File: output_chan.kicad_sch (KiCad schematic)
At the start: 12 parts, among them U2 MAX14917AFM+

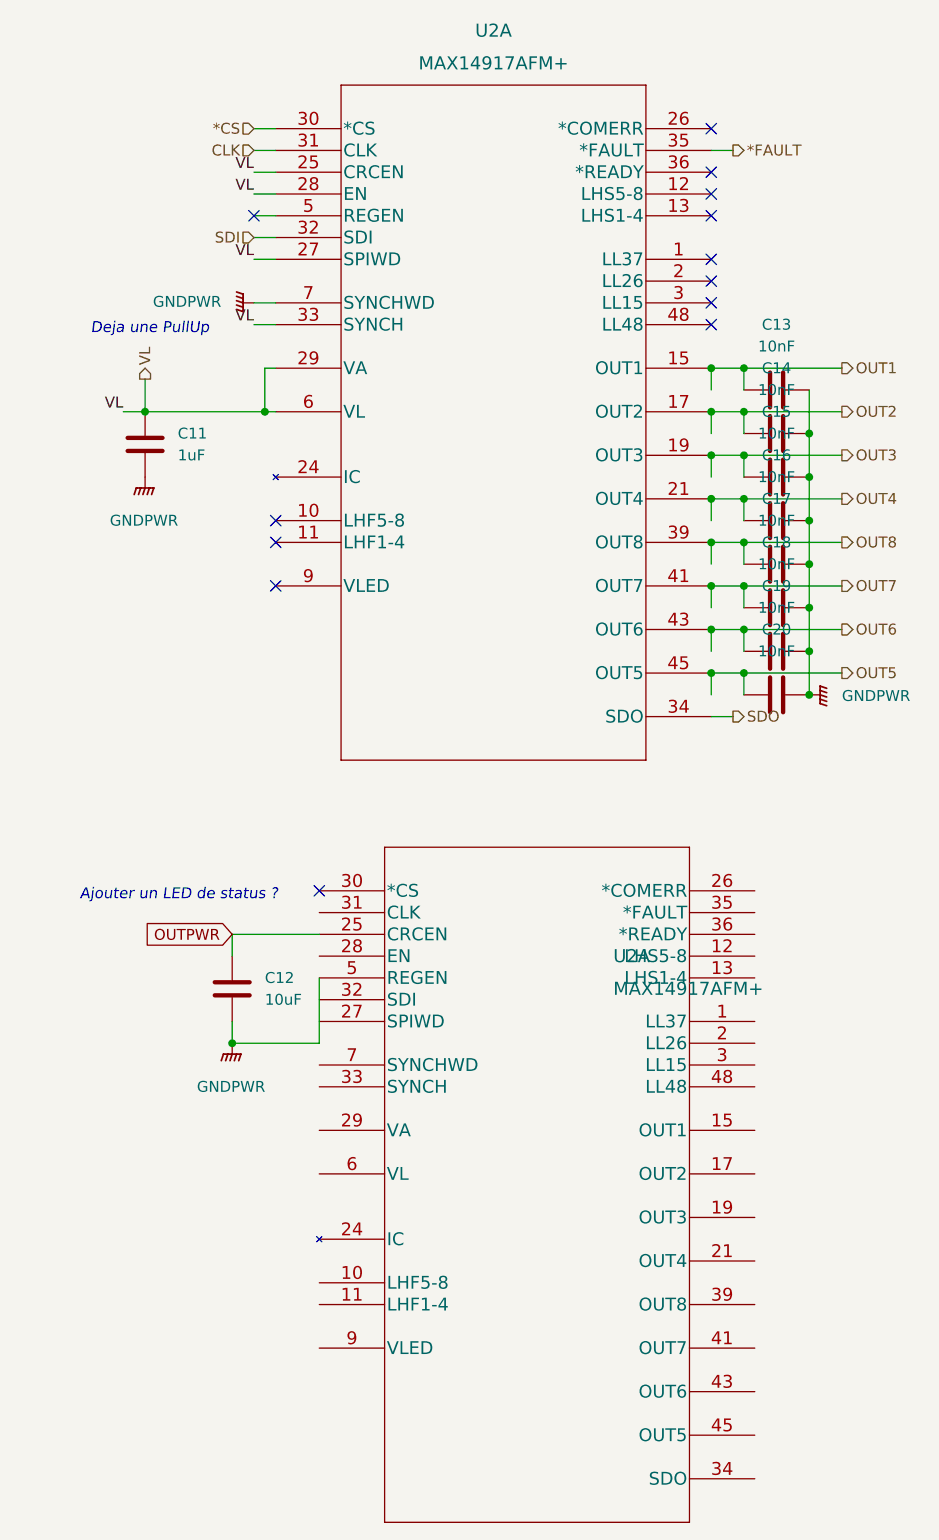
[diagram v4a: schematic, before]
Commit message: Basic routing done, cheating a bit on the diff + add holes (to be positionned)
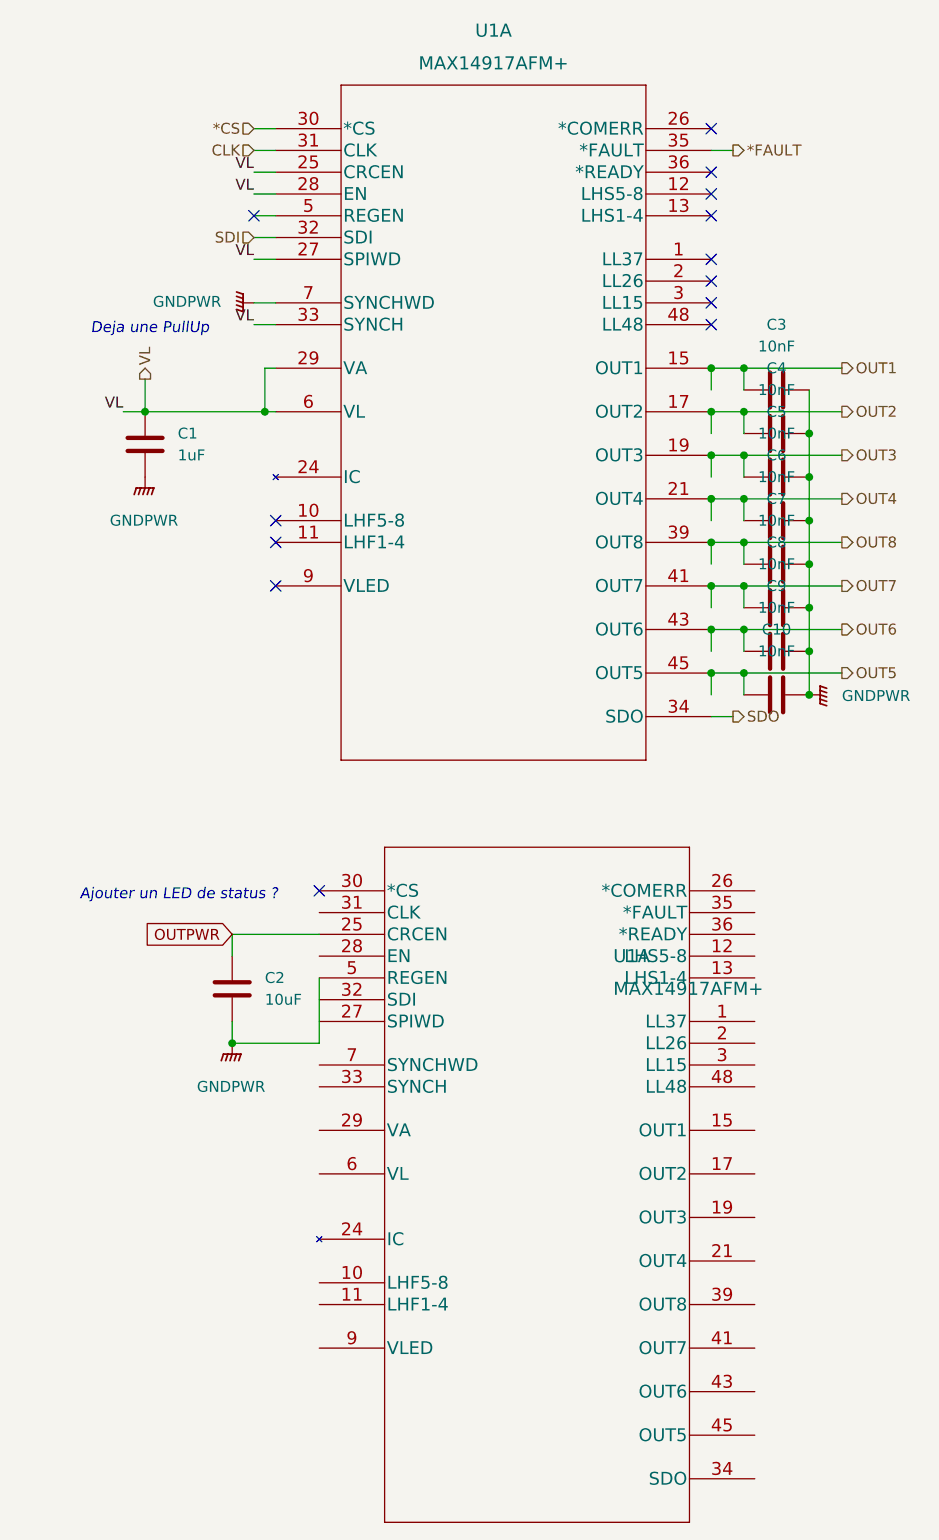
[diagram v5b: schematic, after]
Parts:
- renumbered C11 to C1, C20 to C10, C12 to C2, C13 to C3, C14 to C4, C15 to C5, C16 to C6, C17 to C7, C18 to C8, C19 to C9, U2 to U1
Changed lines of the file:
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@@
   (symbol (lib_id "power:GNDPWR") (at 189.23 109.22 90)
     (in_bom yes) (on_board yes) (fields_autoplaced)
-    (property "Reference" "#PWR08" (id 0) (at 194.31 109.22 0)
+    (property "Reference" "#PWR04" (id 0) (at 194.31 109.22 0)
       (effects (font (size 1.27 1.27)) hide)
     )
@@
   (symbol (lib_id "Device:C") (at 111.76 80.01 0)
     (in_bom yes) (on_board yes) (fields_autoplaced)
-    (property "Reference" "C11" (id 0) (at 115.57 78.7399 0)
+    (property "Reference" "C1" (id 0) (at 115.57 78.7399 0)
       (effects (font (size 1.27 1.27)) (justify left))
     )
@@
   (symbol (lib_id "power:GNDPWR") (at 111.76 83.82 0)
     (in_bom yes) (on_board yes) (fields_autoplaced)
-    (property "Reference" "#PWR05" (id 0) (at 111.76 88.9 0)
+    (property "Reference" "#PWR01" (id 0) (at 111.76 88.9 0)
       (effects (font (size 1.27 1.27)) hide)
     )
@@
   (symbol (lib_id "Maxim industrial IO:MAX14917AFM+") (at 127 43.18 0)
     (in_bom yes) (on_board yes) (fields_autoplaced)
-    (property "Reference" "U2" (id 0) (at 152.4 31.75 0)
+    (property "Reference" "U1" (id 0) (at 152.4 31.75 0)
       (effects (font (size 1.524 1.524)))
     )
@@
   (symbol (lib_id "Device:C") (at 185.42 83.82 90)
     (in_bom yes) (on_board yes) (fields_autoplaced)
-    (property "Reference" "C15" (id 0) (at 185.42 76.2 90))
+    (property "Reference" "C5" (id 0) (at 185.42 76.2 90))
     (property "Value" "10nF" (id 1) (at 185.42 78.74 90))
     (property "Footprint" "Capacitor_SMD:C_0603_1608Metric" (id 2) (at 189.23 82.8548 0)
@@
   (symbol (lib_id "Device:C") (at 185.42 88.9 90)
     (in_bom yes) (on_board yes) (fields_autoplaced)
-    (property "Reference" "C16" (id 0) (at 185.42 81.28 90))
+    (property "Reference" "C6" (id 0) (at 185.42 81.28 90))
     (property "Value" "10nF" (id 1) (at 185.42 83.82 90))
     (property "Footprint" "Capacitor_SMD:C_0603_1608Metric" (id 2) (at 189.23 87.9348 0)
@@
   (symbol (lib_id "Device:C") (at 185.42 78.74 90)
     (in_bom yes) (on_board yes) (fields_autoplaced)
-    (property "Reference" "C14" (id 0) (at 185.42 71.12 90))
+    (property "Reference" "C4" (id 0) (at 185.42 71.12 90))
     (property "Value" "10nF" (id 1) (at 185.42 73.66 90))
     (property "Footprint" "Capacitor_SMD:C_0603_1608Metric" (id 2) (at 189.23 77.7748 0)
@@
   (symbol (lib_id "Device:C") (at 185.42 104.14 90)
     (in_bom yes) (on_board yes) (fields_autoplaced)
-    (property "Reference" "C19" (id 0) (at 185.42 96.52 90))
+    (property "Reference" "C9" (id 0) (at 185.42 96.52 90))
     (property "Value" "10nF" (id 1) (at 185.42 99.06 90))
     (property "Footprint" "Capacitor_SMD:C_0603_1608Metric" (id 2) (at 189.23 103.1748 0)
@@
   (symbol (lib_id "power:GNDPWR") (at 124.46 63.5 270)
     (in_bom yes) (on_board yes) (fields_autoplaced)
-    (property "Reference" "#PWR07" (id 0) (at 119.38 63.5 0)
+    (property "Reference" "#PWR03" (id 0) (at 119.38 63.5 0)
       (effects (font (size 1.27 1.27)) hide)
     )
@@
   (symbol (lib_id "Maxim industrial IO:MAX14917AFM+") (at 132.08 132.08 0)
     (in_bom yes) (on_board yes) (fields_autoplaced)
-    (property "Reference" "U2" (id 0) (at 166.37 139.7 0)
+    (property "Reference" "U1" (id 0) (at 166.37 139.7 0)
       (effects (font (size 1.524 1.524)) (justify left))
     )
@@
       (effects (font (size 1.524 1.524)))
     )
-    (pin "1")
-    (pin "10")
-    (pin "11")
-    (pin "12")
-    (pin "13")
-    (pin "15")
-    (pin "16")
-    (pin "17")
-    (pin "18")
-    (pin "19")
-    (pin "2")
-    (pin "20")
-    (pin "21")
-    (pin "22")
-    (pin "24")
-    (pin "25")
-    (pin "26")
-    (pin "27")
-    (pin "28")
-    (pin "29")
-    (pin "3")
-    (pin "30")
-    (pin "31")
-    (pin "32")
-    (pin "33")
-    (pin "34")
-    (pin "35")
-    (pin "36")
-    (pin "37")
-    (pin "39")
-    (pin "40")
-    (pin "41")
-    (pin "42")
-    (pin "43")
-    (pin "44")
-    (pin "45")
-    (pin "46")
-    (pin "48")
-    (pin "5")
-    (pin "6")
-    (pin "7")
-    (pin "9")
+    (pin "14")
+    (pin "23")
+    (pin "38")
+    (pin "4")
+    (pin "47")
+    (pin "49")
+    (pin "8")
   )
   (symbol (lib_id "Device:C") (at 185.42 93.98 90)
     (in_bom yes) (on_board yes) (fields_autoplaced)
-    (property "Reference" "C17" (id 0) (at 185.42 86.36 90))
+    (property "Reference" "C7" (id 0) (at 185.42 86.36 90))
     (property "Value" "10nF" (id 1) (at 185.42 88.9 90))
     (property "Footprint" "Capacitor_SMD:C_0603_1608Metric" (id 2) (at 189.23 93.0148 0)
@@
   (symbol (lib_id "Device:C") (at 185.42 73.66 90)
     (in_bom yes) (on_board yes) (fields_autoplaced)
-    (property "Reference" "C13" (id 0) (at 185.42 66.04 90))
+    (property "Reference" "C3" (id 0) (at 185.42 66.04 90))
     (property "Value" "10nF" (id 1) (at 185.42 68.58 90))
     (property "Footprint" "Capacitor_SMD:C_0603_1608Metric" (id 2) (at 189.23 72.6948 0)
@@
   (symbol (lib_id "Device:C") (at 185.42 99.06 90)
     (in_bom yes) (on_board yes) (fields_autoplaced)
-    (property "Reference" "C18" (id 0) (at 185.42 91.44 90))
+    (property "Reference" "C8" (id 0) (at 185.42 91.44 90))
     (property "Value" "10nF" (id 1) (at 185.42 93.98 90))
     (property "Footprint" "Capacitor_SMD:C_0603_1608Metric" (id 2) (at 189.23 98.0948 0)
@@
   (symbol (lib_id "power:GNDPWR") (at 121.92 149.86 0)
     (in_bom yes) (on_board yes) (fields_autoplaced)
-    (property "Reference" "#PWR06" (id 0) (at 121.92 154.94 0)
+    (property "Reference" "#PWR02" (id 0) (at 121.92 154.94 0)
       (effects (font (size 1.27 1.27)) hide)
     )
@@
   (symbol (lib_id "Device:C") (at 121.92 143.51 0)
     (in_bom yes) (on_board yes) (fields_autoplaced)
-    (property "Reference" "C12" (id 0) (at 125.73 142.2399 0)
+    (property "Reference" "C2" (id 0) (at 125.73 142.2399 0)
       (effects (font (size 1.27 1.27)) (justify left))
     )
@@
   (symbol (lib_id "Device:C") (at 185.42 109.22 90)
     (in_bom yes) (on_board yes) (fields_autoplaced)
-    (property "Reference" "C20" (id 0) (at 185.42 101.6 90))
+    (property "Reference" "C10" (id 0) (at 185.42 101.6 90))
     (property "Value" "10nF" (id 1) (at 185.42 104.14 90))
     (property "Footprint" "Capacitor_SMD:C_0603_1608Metric" (id 2) (at 189.23 108.2548 0)

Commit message: fix most errors/warnings
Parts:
- renumbered C1 to C23, C2 to C24, C3 to C25, C4 to C26, C5 to C27, C6 to C28, C7 to C29, C8 to C30, C9 to C31, C10 to C32, U1 to U4
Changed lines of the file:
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@@
   (symbol (lib_id "Device:C") (at 111.76 80.01 0)
     (in_bom yes) (on_board yes) (fields_autoplaced)
-    (property "Reference" "C1" (id 0) (at 115.57 78.7399 0)
+    (property "Reference" "C23" (id 0) (at 115.57 78.7399 0)
       (effects (font (size 1.27 1.27)) (justify left))
     )
@@
   (symbol (lib_id "Maxim industrial IO:MAX14917AFM+") (at 127 43.18 0)
     (in_bom yes) (on_board yes) (fields_autoplaced)
-    (property "Reference" "U1" (id 0) (at 152.4 31.75 0)
+    (property "Reference" "U4" (id 0) (at 152.4 31.75 0)
       (effects (font (size 1.524 1.524)))
     )
@@
   (symbol (lib_id "Device:C") (at 185.42 83.82 90)
     (in_bom yes) (on_board yes) (fields_autoplaced)
-    (property "Reference" "C5" (id 0) (at 185.42 76.2 90))
+    (property "Reference" "C27" (id 0) (at 185.42 76.2 90))
     (property "Value" "10nF" (id 1) (at 185.42 78.74 90))
     (property "Footprint" "Capacitor_SMD:C_0603_1608Metric" (id 2) (at 189.23 82.8548 0)
@@
   (symbol (lib_id "Device:C") (at 185.42 88.9 90)
     (in_bom yes) (on_board yes) (fields_autoplaced)
-    (property "Reference" "C6" (id 0) (at 185.42 81.28 90))
+    (property "Reference" "C28" (id 0) (at 185.42 81.28 90))
     (property "Value" "10nF" (id 1) (at 185.42 83.82 90))
     (property "Footprint" "Capacitor_SMD:C_0603_1608Metric" (id 2) (at 189.23 87.9348 0)
@@
   (symbol (lib_id "Device:C") (at 185.42 78.74 90)
     (in_bom yes) (on_board yes) (fields_autoplaced)
-    (property "Reference" "C4" (id 0) (at 185.42 71.12 90))
+    (property "Reference" "C26" (id 0) (at 185.42 71.12 90))
     (property "Value" "10nF" (id 1) (at 185.42 73.66 90))
     (property "Footprint" "Capacitor_SMD:C_0603_1608Metric" (id 2) (at 189.23 77.7748 0)
@@
   (symbol (lib_id "Device:C") (at 185.42 104.14 90)
     (in_bom yes) (on_board yes) (fields_autoplaced)
-    (property "Reference" "C9" (id 0) (at 185.42 96.52 90))
+    (property "Reference" "C31" (id 0) (at 185.42 96.52 90))
     (property "Value" "10nF" (id 1) (at 185.42 99.06 90))
     (property "Footprint" "Capacitor_SMD:C_0603_1608Metric" (id 2) (at 189.23 103.1748 0)
@@
   (symbol (lib_id "Maxim industrial IO:MAX14917AFM+") (at 132.08 132.08 0)
     (in_bom yes) (on_board yes) (fields_autoplaced)
-    (property "Reference" "U1" (id 0) (at 166.37 139.7 0)
+    (property "Reference" "U4" (id 0) (at 166.37 139.7 0)
       (effects (font (size 1.524 1.524)) (justify left))
     )
@@
   (symbol (lib_id "Device:C") (at 185.42 93.98 90)
     (in_bom yes) (on_board yes) (fields_autoplaced)
-    (property "Reference" "C7" (id 0) (at 185.42 86.36 90))
+    (property "Reference" "C29" (id 0) (at 185.42 86.36 90))
     (property "Value" "10nF" (id 1) (at 185.42 88.9 90))
     (property "Footprint" "Capacitor_SMD:C_0603_1608Metric" (id 2) (at 189.23 93.0148 0)
@@
   (symbol (lib_id "Device:C") (at 185.42 73.66 90)
     (in_bom yes) (on_board yes) (fields_autoplaced)
-    (property "Reference" "C3" (id 0) (at 185.42 66.04 90))
+    (property "Reference" "C25" (id 0) (at 185.42 66.04 90))
     (property "Value" "10nF" (id 1) (at 185.42 68.58 90))
     (property "Footprint" "Capacitor_SMD:C_0603_1608Metric" (id 2) (at 189.23 72.6948 0)
@@
   (symbol (lib_id "Device:C") (at 185.42 99.06 90)
     (in_bom yes) (on_board yes) (fields_autoplaced)
-    (property "Reference" "C8" (id 0) (at 185.42 91.44 90))
+    (property "Reference" "C30" (id 0) (at 185.42 91.44 90))
     (property "Value" "10nF" (id 1) (at 185.42 93.98 90))
     (property "Footprint" "Capacitor_SMD:C_0603_1608Metric" (id 2) (at 189.23 98.0948 0)
@@
   (symbol (lib_id "Device:C") (at 121.92 143.51 0)
     (in_bom yes) (on_board yes) (fields_autoplaced)
-    (property "Reference" "C2" (id 0) (at 125.73 142.2399 0)
+    (property "Reference" "C24" (id 0) (at 125.73 142.2399 0)
       (effects (font (size 1.27 1.27)) (justify left))
     )
@@
   (symbol (lib_id "Device:C") (at 185.42 109.22 90)
     (in_bom yes) (on_board yes) (fields_autoplaced)
-    (property "Reference" "C10" (id 0) (at 185.42 101.6 90))
+    (property "Reference" "C32" (id 0) (at 185.42 101.6 90))
     (property "Value" "10nF" (id 1) (at 185.42 104.14 90))
     (property "Footprint" "Capacitor_SMD:C_0603_1608Metric" (id 2) (at 189.23 108.2548 0)
